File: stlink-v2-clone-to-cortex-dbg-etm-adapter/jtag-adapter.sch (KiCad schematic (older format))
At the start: 3 parts, among them J1 Conn_02x05_Odd_Even, J2 Conn_02x10_Odd_Even

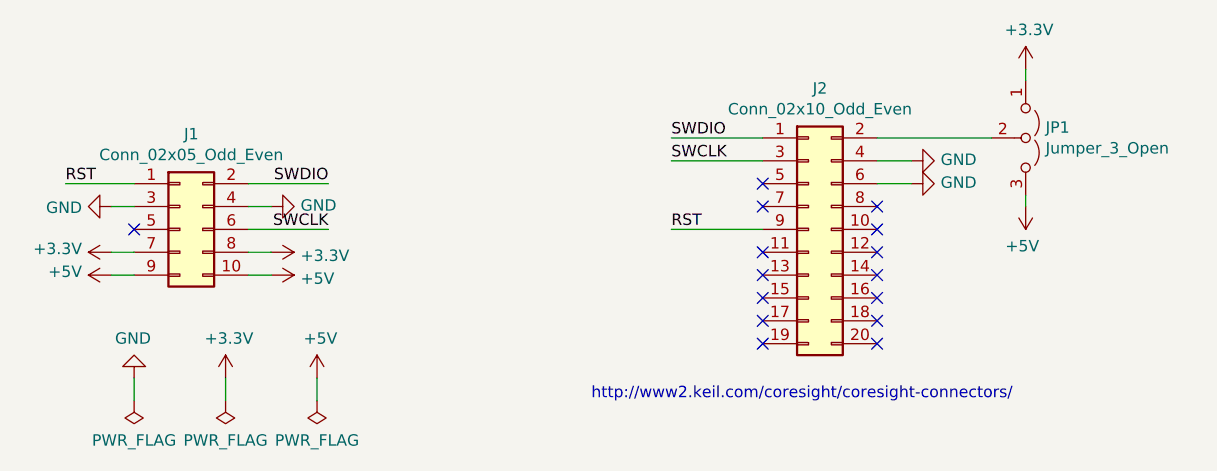
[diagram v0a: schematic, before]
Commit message: [stlinkv2-jtagetm-adapter] Change header to socket for 20pin connector. Update README.
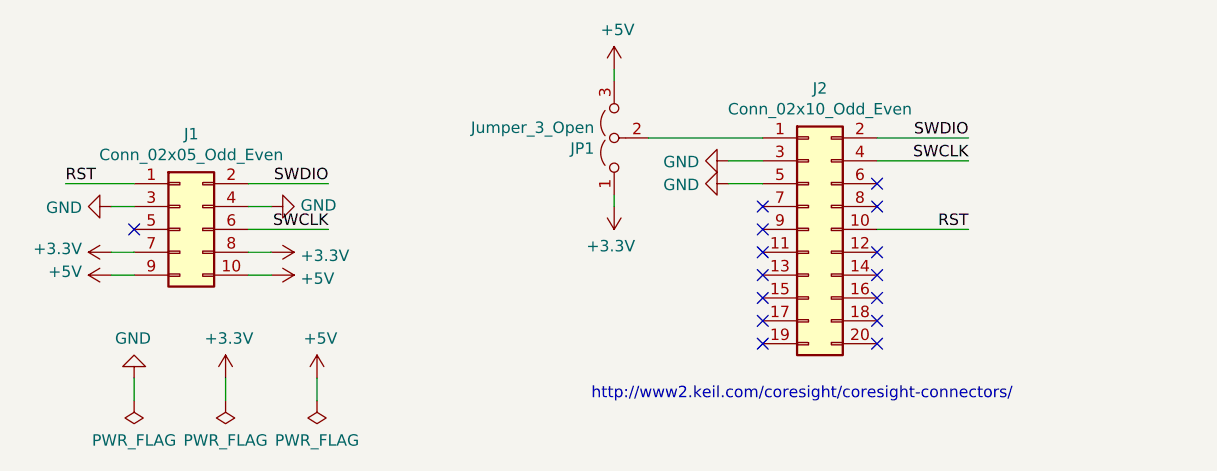
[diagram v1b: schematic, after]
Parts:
- J2: footprint Connector_PinHeader_1.27mm:PinHeader_2x10_P1.27mm_Vertical_SMD -> Connector_PinSocket_1.27mm:PinSocket_2x10_P1.27mm_Vertical_SMD
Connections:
- net GND: now also J2.3 (Pin_3), J2.5 (Pin_5); no longer J2.4 (Pin_4), J2.6 (Pin_6)
- net RST: now also J2.10 (Pin_10); no longer J2.9 (Pin_9)
- net SWCLK: now also J2.4 (Pin_4); no longer J2.3 (Pin_3)
- net SWDIO: now also J2.2 (Pin_2); no longer J2.1 (Pin_1)
- net at JP1.2 (C): now also J2.1 (Pin_1); no longer J2.2 (Pin_2)
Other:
- moved on the sheet: JP1
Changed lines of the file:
@@
 Text Notes 6150 4100 0    50   ~ 0
 http://www2.keil.com/coresight/coresight-connectors/
-Text Label 6500 2950 0    50   ~ 0
+Text Label 7800 2950 2    50   ~ 0
 SWDIO
-Text Label 6500 3050 0    50   ~ 0
+Text Label 7800 3050 2    50   ~ 0
 SWCLK
-Text Label 6500 3350 0    50   ~ 0
+Text Label 7800 3350 2    50   ~ 0
 RST
 $Comp
 L power:GND #PWR0107
 U 1 1 5F27E242
-P 7550 3050
-F 0 "#PWR0107" H 7550 2800 50  0001 C CNN
-F 1 "GND" V 7555 2922 50  0000 R CNN
-F 2 "" H 7550 3050 50  0001 C CNN
-F 3 "" H 7550 3050 50  0001 C CNN
-	1    7550 3050
-	0    -1   -1   0
+P 6750 3150
+F 0 "#PWR0107" H 6750 2900 50  0001 C CNN
+F 1 "GND" V 6755 3022 50  0000 R CNN
+F 2 "" H 6750 3150 50  0001 C CNN
+F 3 "" H 6750 3150 50  0001 C CNN
+	1    6750 3150
+	0    1    1    0
 $EndComp
 $Comp
 L power:GND #PWR0108
 U 1 1 5F27E72C
-P 7550 3150
-F 0 "#PWR0108" H 7550 2900 50  0001 C CNN
-F 1 "GND" V 7555 3022 50  0000 R CNN
-F 2 "" H 7550 3150 50  0001 C CNN
-F 3 "" H 7550 3150 50  0001 C CNN
-	1    7550 3150
-	0    -1   -1   0
+P 6750 3050
+F 0 "#PWR0108" H 6750 2800 50  0001 C CNN
+F 1 "GND" V 6755 2922 50  0000 R CNN
+F 2 "" H 6750 3050 50  0001 C CNN
+F 3 "" H 6750 3050 50  0001 C CNN
+	1    6750 3050
+	0    1    1    0
 $EndComp
 Wire Wire Line
-	6900 3050 6500 3050
+	7800 3050 7400 3050
 Wire Wire Line
-	6500 2950 6900 2950
-Wire Wire Line
-	7900 2950 7400 2950
-$Comp
-L Jumper:Jumper_3_Open JP1
-U 1 1 5F2821FC
-P 8050 2950
-F 0 "JP1" V 8004 3037 50  0000 L CNN
-F 1 "Jumper_3_Open" V 8095 3037 50  0000 L CNN
-F 2 "Connector_PinHeader_1.27mm:PinHeader_1x03_P1.27mm_Vertical" H 8050 2950 50  0001 C CNN
-F 3 "~" H 8050 2950 50  0001 C CNN
-	1    8050 2950
-	0    1    1    0
-$EndComp
-$Comp
-L power:+5V #PWR0109
-U 1 1 5F2855A9
-P 8050 3250
-F 0 "#PWR0109" H 8050 3100 50  0001 C CNN
-F 1 "+5V" H 8065 3423 50  0000 C CNN
-F 2 "" H 8050 3250 50  0001 C CNN
-F 3 "" H 8050 3250 50  0001 C CNN
-	1    8050 3250
-	-1   0    0    1
-$EndComp
-$Comp
-L power:+3.3V #PWR0110
-U 1 1 5F285F46
-P 8050 2650
-F 0 "#PWR0110" H 8050 2500 50  0001 C CNN
-F 1 "+3.3V" H 8065 2823 50  0000 C CNN
-F 2 "" H 8050 2650 50  0001 C CNN
-F 3 "" H 8050 2650 50  0001 C CNN
-	1    8050 2650
-	1    0    0    -1
-$EndComp
-Wire Wire Line
-	8050 2650 8050 2700
-Wire Wire Line
-	8050 3200 8050 3250
+	7400 2950 7800 2950
 NoConn ~ 7400 3250
 NoConn ~ 7400 3450
@@
 	4950 4000 4950 4100
 Wire Wire Line
-	7550 3050 7400 3050
+	6750 3150 6900 3150
 $Comp
 L Connector_Generic:Conn_02x10_Odd_Even J2
@@
 F 0 "J2" H 7150 3967 50  0000 C CNN
 F 1 "Conn_02x10_Odd_Even" H 7150 3876 50  0000 C CNN
-F 2 "Connector_PinHeader_1.27mm:PinHeader_2x10_P1.27mm_Vertical_SMD" H 7100 3350 50  0001 C CNN
+F 2 "Connector_PinSocket_1.27mm:PinSocket_2x10_P1.27mm_Vertical_SMD" H 7100 3350 50  0001 C CNN
 F 3 "~" H 7100 3350 50  0001 C CNN
 	1    7100 3350
@@
 $EndComp
 Wire Wire Line
-	7400 3150 7550 3150
+	6900 3050 6750 3050
 Wire Wire Line
-	6500 3350 6900 3350
-NoConn ~ 6900 3150
-NoConn ~ 7400 3350
+	7400 3350 7800 3350
+Wire Wire Line
+	6250 2700 6250 2650
+Wire Wire Line
+	6250 3250 6250 3200
+$Comp
+L power:+3.3V #PWR0110
+U 1 1 5F285F46
+P 6250 3250
+F 0 "#PWR0110" H 6250 3100 50  0001 C CNN
+F 1 "+3.3V" H 6265 3423 50  0000 C CNN
+F 2 "" H 6250 3250 50  0001 C CNN
+F 3 "" H 6250 3250 50  0001 C CNN
+	1    6250 3250
+	-1   0    0    1
+$EndComp
+$Comp
+L power:+5V #PWR0109
+U 1 1 5F2855A9
+P 6250 2650
+F 0 "#PWR0109" H 6250 2500 50  0001 C CNN
+F 1 "+5V" H 6265 2823 50  0000 C CNN
+F 2 "" H 6250 2650 50  0001 C CNN
+F 3 "" H 6250 2650 50  0001 C CNN
+	1    6250 2650
+	1    0    0    -1
+$EndComp
+$Comp
+L Jumper:Jumper_3_Open JP1
+U 1 1 5F2821FC
+P 6250 2950
+F 0 "JP1" V 6204 3037 50  0000 L CNN
+F 1 "Jumper_3_Open" V 6295 3037 50  0000 L CNN
+F 2 "Connector_PinHeader_1.27mm:PinHeader_1x03_P1.27mm_Vertical" H 6250 2950 50  0001 C CNN
+F 3 "~" H 6250 2950 50  0001 C CNN
+	1    6250 2950
+	0    -1   -1   0
+$EndComp
+Wire Wire Line
+	6900 2950 6400 2950
+NoConn ~ 7400 3150
+NoConn ~ 6900 3350
 $EndSCHEMATC
